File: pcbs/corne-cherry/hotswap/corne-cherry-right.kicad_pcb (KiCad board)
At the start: 2 copper layers, 160 x 109.4 mm, 47 parts, among them U1 rp2040

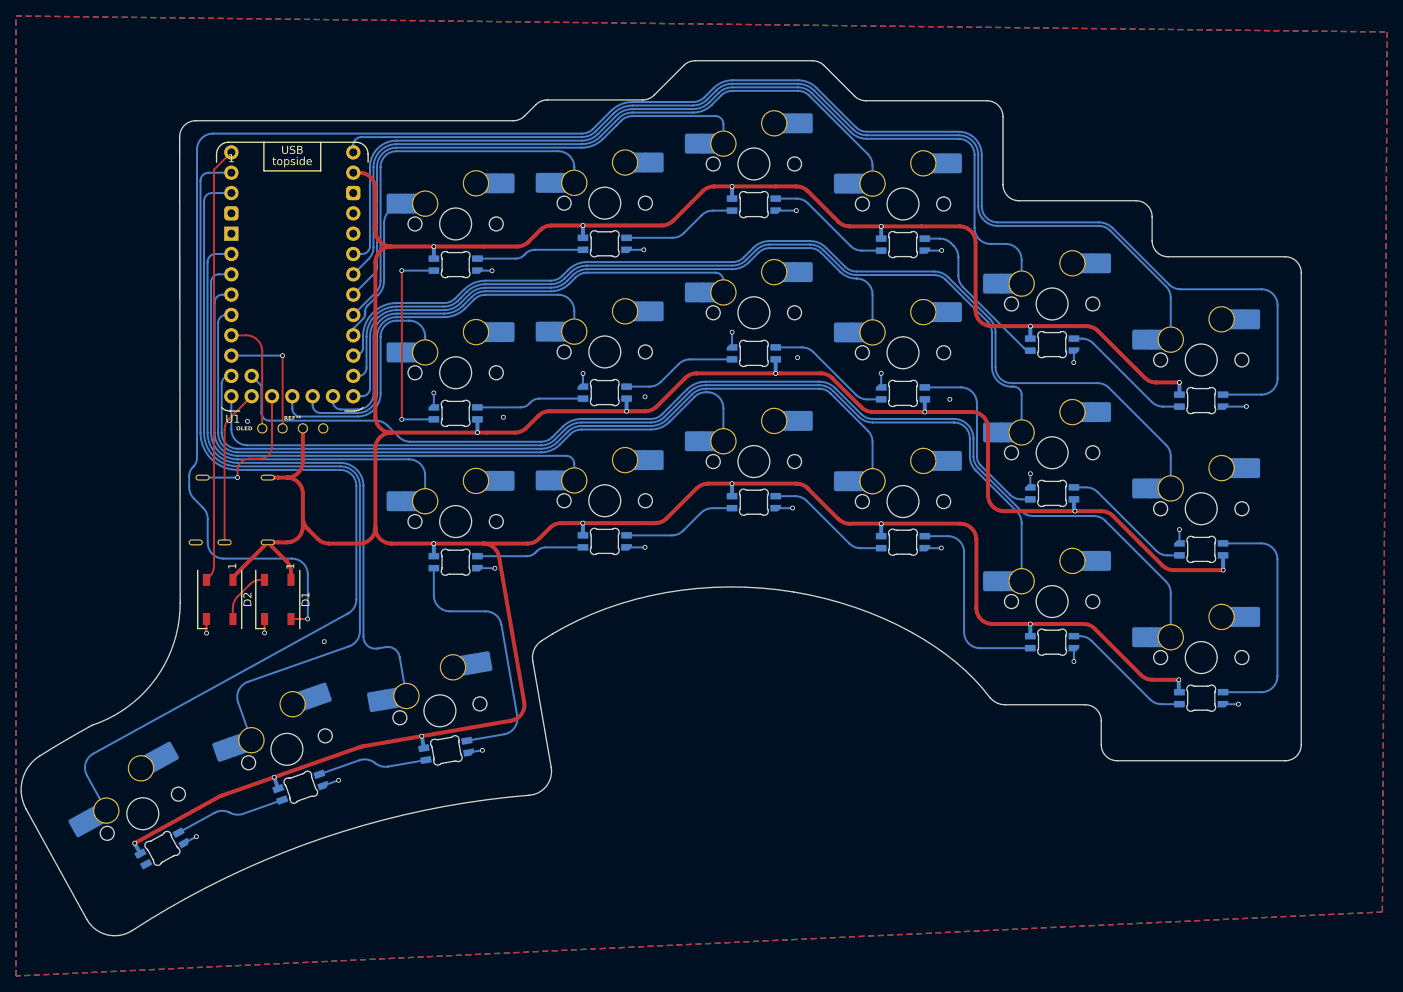
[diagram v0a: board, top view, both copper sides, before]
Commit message: split into left and right
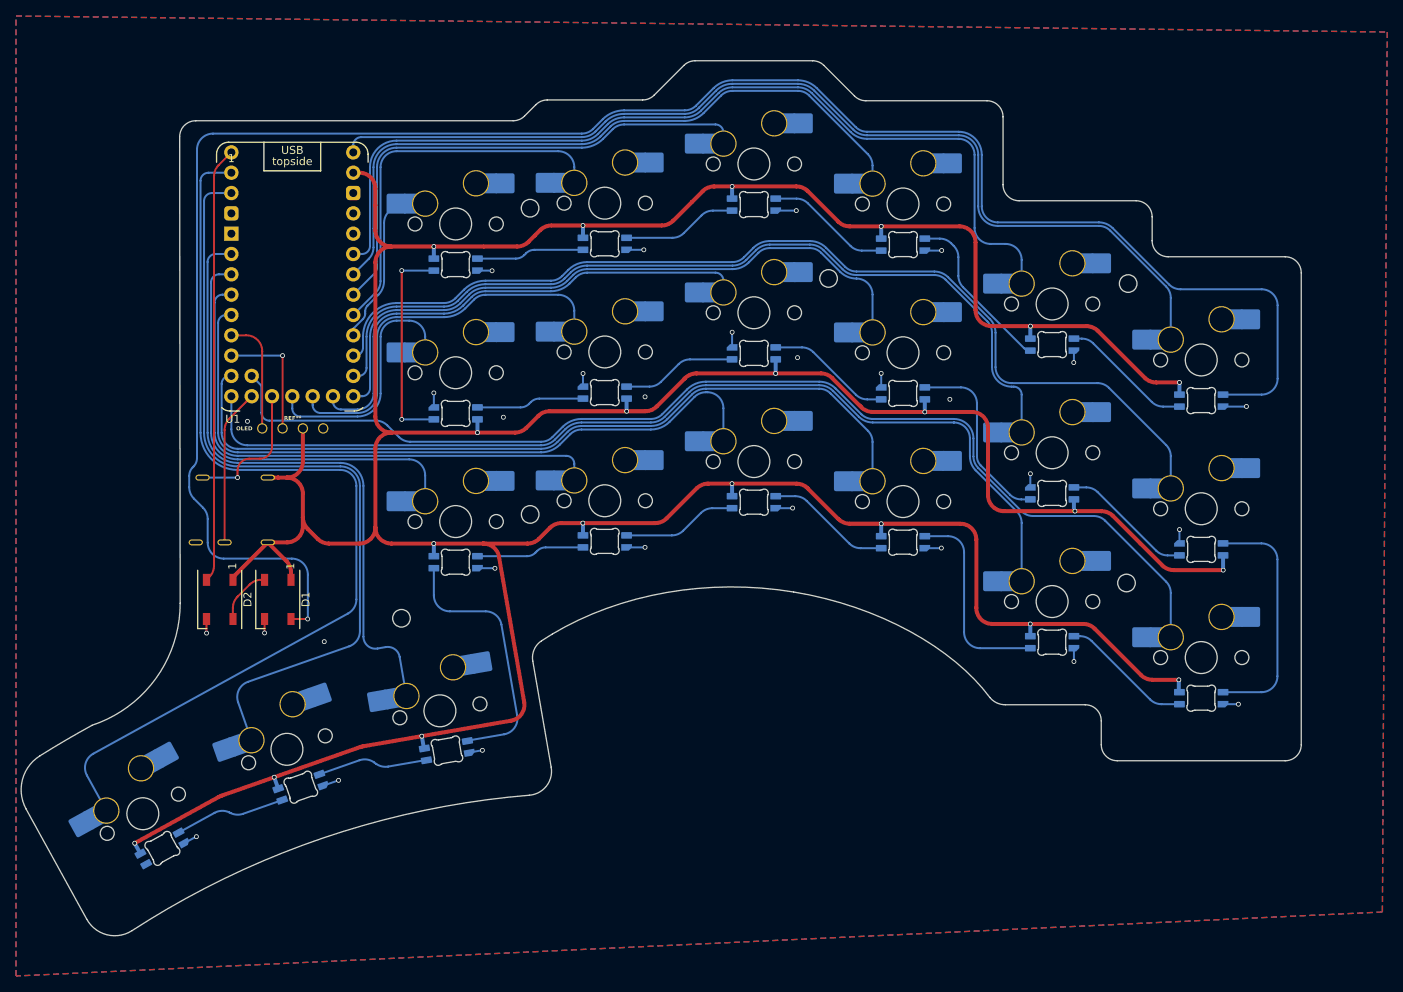
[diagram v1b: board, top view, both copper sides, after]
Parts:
- added REF**: MountingHole_2.2mm_M2, MountingHole:MountingHole_2.2mm_M2, F.Cu at (262.2, 171.6)
- added REF**: MountingHole_2.2mm_M2, MountingHole:MountingHole_2.2mm_M2, F.Cu at (315.6, 129.1)
- added REF**: MountingHole_2.2mm_M2, MountingHole:MountingHole_2.2mm_M2, F.Cu at (352.9, 167.1)
- added REF**: MountingHole_2.2mm_M2, MountingHole:MountingHole_2.2mm_M2, F.Cu at (353.1, 129.7)
- added REF**: MountingHole_2.2mm_M2, MountingHole:MountingHole_2.2mm_M2, F.Cu at (278.3, 120.3)
- added REF**: MountingHole_2.2mm_M2, MountingHole:MountingHole_2.2mm_M2, F.Cu at (278.3, 158.6)
- moved LED57 5.08 mm to (287.7, 156.9)
- moved LED61 5.04 mm to (267.1, 183.1)
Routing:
- net /right/KEY12: track 66.0 -> 64.6 mm

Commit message: add skqg
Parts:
- removed rJ2: ST-0277D00-052-142, kbd_local:ST-0277D00-052-142
- added REF**: SW_SPST_SKQG_WithStem, PCM_marbastlib-various:SW_SPST_SKQG_WithStem, B.Cu at (248.6, 120.7)
- added TRRS: PJ-320A, PJ-320A_Library:PJ-320A, F.Cu at (232.6, 155.8)
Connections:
- U1 pad rst: (no net) -> rst
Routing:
- net rst: track 0.00 -> 11.5 mm
- net GNDR: track 44.9 -> 56.2 mm
- net /right/TX: track 19.6 -> 13.1 mm
- net /right/RX: track 17.4 -> 18.5 mm
- net +5VR: track 561.6 -> 562.3 mm
